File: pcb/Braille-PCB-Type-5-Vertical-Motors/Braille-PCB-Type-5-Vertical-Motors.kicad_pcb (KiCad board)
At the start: 2 copper layers, 90 x 90 mm, 113 parts, among them J1 Screw_Terminal_01x02, J10 Conn_01x02, J11 Conn_01x02, J12 Conn_01x02, J13 Conn_01x02, J14 Conn_01x02, J15 Conn_01x02, J16 Conn_01x02, J17 Conn_01x02, J18 Conn_01x02, J19 Conn_01x02, J2 Screw_Terminal_01x02, J20 Conn_01x02, J3 Screw_Terminal_01x02, J4 Conn_01x03, J5 Conn_01x02, J6 Conn_01x08, J7 Jumper-3-Way-Power, J8 Barrel_Jack_Switch, J9 Conn_01x02, M1 Motor_DC, M10 Motor_DC, M11 Motor_DC, M12 Motor_DC, M2 Motor_DC, M3 Motor_DC, M4 Motor_DC, M5 Motor_DC, M6 Motor_DC, M7 Motor_DC, M8 Motor_DC, M9 Motor_DC, SW1 SW_Push, SW2 SW_Push, U1 RP2040-Zero, U10 AD116, U14 AD116, U15 AD116, U16 AD116, U2 AD116, U20 AD116, U21 AD116, U22 AD116, U26 74HC595, U27 74HC595, U28 74HC595, U3 AD116, U32 AMS1117-3.3, U4 AD116, U8 AD116, U9 AD116

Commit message: PCB WIP: Add motor shaft holes
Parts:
- added H13: MountingHole, 00-project-footprints:Hole_for_Motor_Shaft, F.Cu at (52.7, 47.4)
- added H14: MountingHole, 00-project-footprints:Hole_for_Motor_Shaft, F.Cu at (154.9, 72.3)
- added H15: MountingHole, 00-project-footprints:Hole_for_Motor_Shaft, F.Cu at (162.7, 72.3)
- added H16: MountingHole, 00-project-footprints:Hole_for_Motor_Shaft, F.Cu at (170.4, 72.3)
- added H17: MountingHole, 00-project-footprints:Hole_for_Motor_Shaft, F.Cu at (49.7, 50.0)
- added H18: MountingHole, 00-project-footprints:Hole_for_Motor_Shaft, F.Cu at (154.9, 78.0)
- added H19: MountingHole, 00-project-footprints:Hole_for_Motor_Shaft, F.Cu at (162.7, 78.0)
- added H20: MountingHole, 00-project-footprints:Hole_for_Motor_Shaft, F.Cu at (170.4, 78.0)
- added H21: MountingHole, 00-project-footprints:Hole_for_Motor_Shaft, F.Cu at (52.7, 52.6)
- added H22: MountingHole, 00-project-footprints:Hole_for_Motor_Shaft, F.Cu at (154.9, 83.8)
- added H23: MountingHole, 00-project-footprints:Hole_for_Motor_Shaft, F.Cu at (162.7, 83.8)
- added H24: MountingHole, 00-project-footprints:Hole_for_Motor_Shaft, F.Cu at (170.4, 83.8)
- D1, D26, D27: footprint LED_SMD:LED_1206_3216Metric_Pad1.42x1.75mm_HandSolder -> LED_SMD:LED_0603_1608Metric_Pad1.05x0.95mm_HandSolder
- moved J19 117.8 mm to (63.2, 69.5), turned to -90 degrees
- moved J15 113.0 mm to (63.2, 65.5), turned to -90 degrees
- moved J11 108.2 mm to (63.2, 61.5), turned to -90 degrees
- moved J20 100.0 mm to (69.2, 69.5), turned to -90 degrees
- moved J16 95.3 mm to (69.2, 65.5), turned to -90 degrees
- moved M3 93.6 mm to (61.7, 47.4), turned to 180 degrees
- moved M7 90.9 mm to (64.7, 50.0), turned to 180 degrees
- moved J18 90.7 mm to (57.2, 69.5), turned to -90 degrees
- moved J12 90.7 mm to (69.2, 61.5), turned to -90 degrees
- moved M11 89.0 mm to (61.7, 52.6), turned to 180 degrees
- moved J14 86.4 mm to (57.2, 65.5), turned to -90 degrees
- moved J10 82.4 mm to (57.2, 61.5), turned to -90 degrees
- moved M4 76.1 mm to (67.7, 47.4), turned to 180 degrees
- moved M8 73.6 mm to (70.7, 50.0), turned to 180 degrees
- moved M12 71.5 mm to (67.7, 52.6), turned to 180 degrees
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
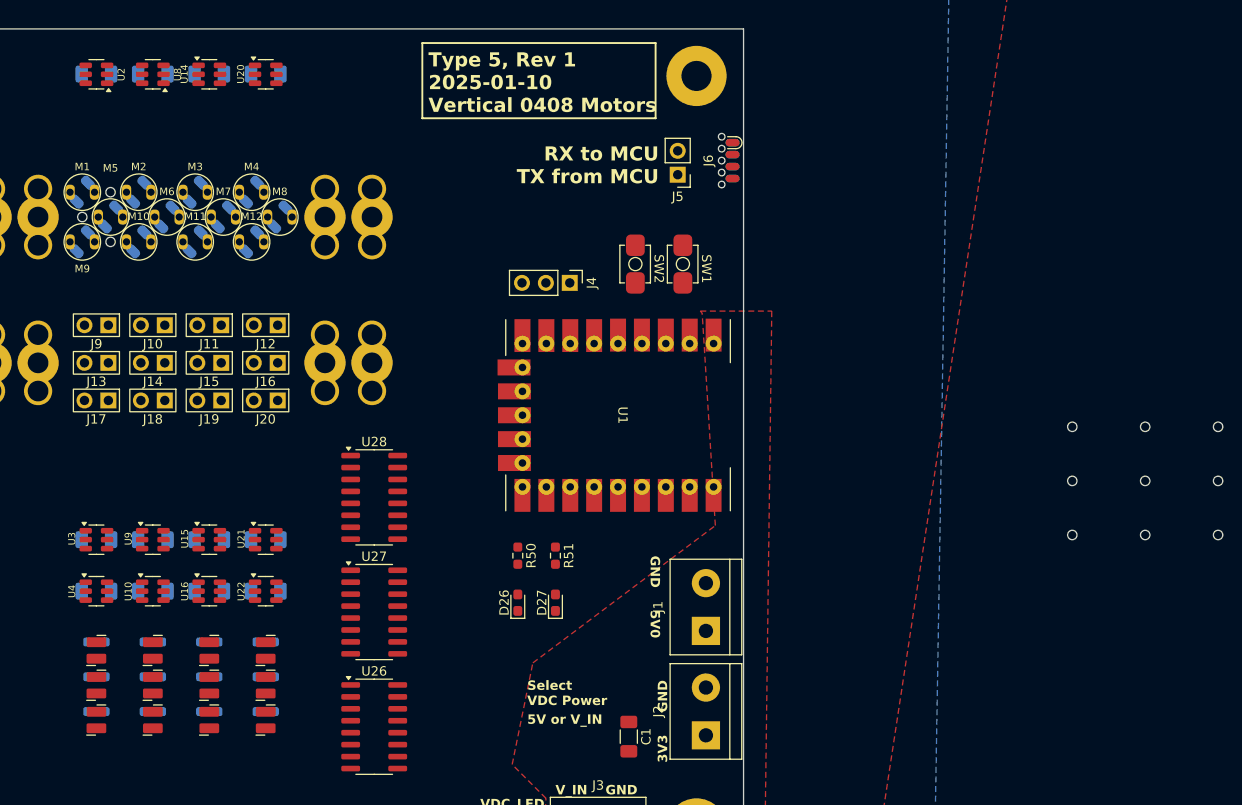
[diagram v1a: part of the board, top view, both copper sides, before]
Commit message: PCB WIP: More layout
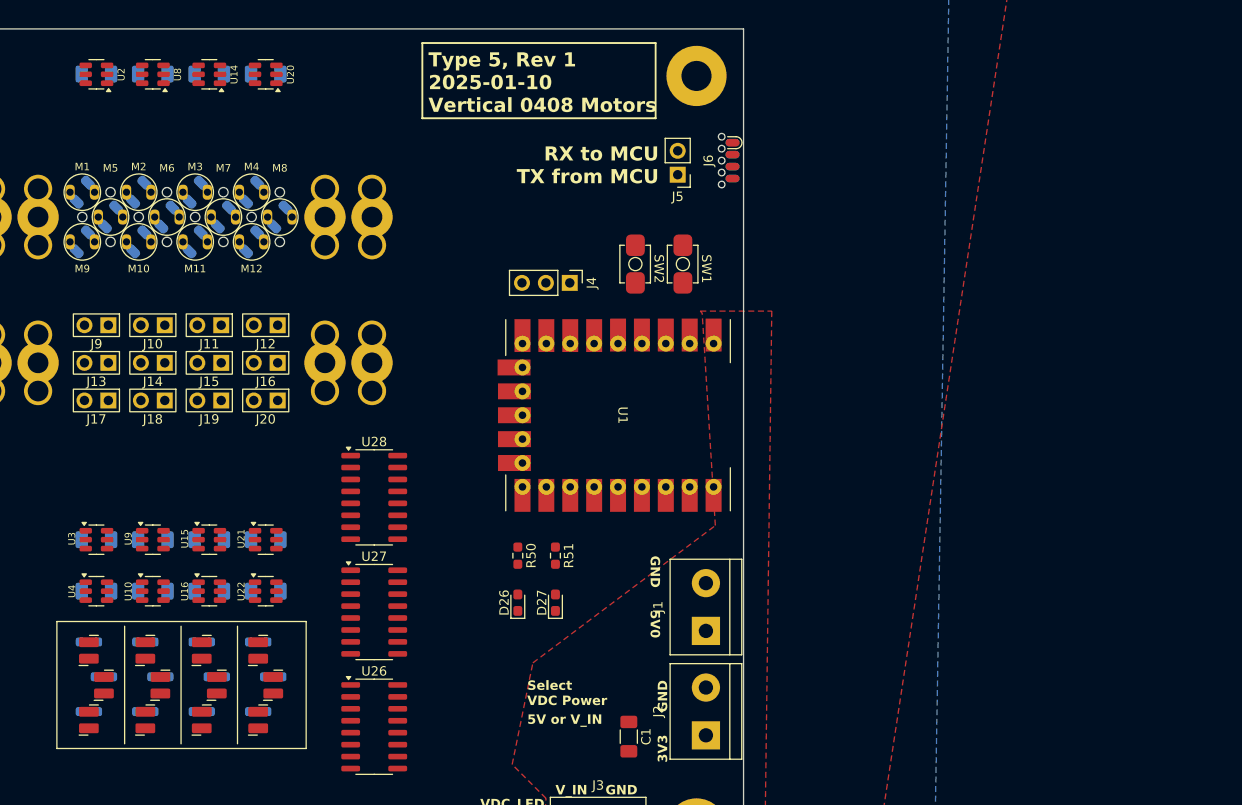
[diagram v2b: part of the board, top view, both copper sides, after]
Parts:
- moved H20 106.5 mm to (67.7, 50.0)
- moved H19 104.8 mm to (61.7, 50.0)
- moved H24 104.5 mm to (70.7, 52.6)
- moved H18 103.1 mm to (55.7, 50.0)
- moved H23 102.8 mm to (64.7, 52.6)
- moved H16 102.8 mm to (70.7, 47.4)
- moved H22 101.2 mm to (58.7, 52.6)
- moved H15 101.1 mm to (64.7, 47.4)
- moved H14 99.4 mm to (58.7, 47.4)
- moved D10 0.80 mm to (56.4, 103.5)
- moved D14 0.80 mm to (62.4, 96.1)
- moved D16 0.80 mm to (62.4, 103.5)
- moved D2 0.80 mm to (50.4, 96.1)
- moved D4 0.80 mm to (50.4, 103.5)
- moved D8 0.80 mm to (56.4, 96.1)
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
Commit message: PCB: Add cross-PCB connectors
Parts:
- added J21: Conn_01x05, 00-project-footprints:PinHeader_1x05_P2.54mm_Vertical_Tight_Centered, F.Cu at (85.5, 50.0)
- added J22: Conn_01x05, 00-project-footprints:PinHeader_1x05_P2.54mm_Vertical_Tight_Centered, F.Cu at (88.5, 50.0)
- added J23: Conn_01x05, 00-project-footprints:PinHeader_1x05_P2.54mm_Vertical_Tight_Centered, F.Cu at (32.0, 50.0)
- added J24: Conn_01x05, 00-project-footprints:PinHeader_1x05_P2.54mm_Vertical_Tight_Centered, F.Cu at (35.0, 50.0)
- moved C31 107.6 mm to (86.6, 99.5)
- moved C30 98.1 mm to (86.6, 87.5)
- moved C27 88.2 mm to (86.6, 75.0)
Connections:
- U28 pad 9: unconnected-(U28-QH'-Pad9) -> /SHIFT_SER_OUT
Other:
- board text added: "IN"
- board text added: "OUT"

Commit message: PCB: Finish setting up power planes
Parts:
- H1, H2, H3, H4: footprint MountingHole:MountingHole_3.2mm_M3_Pad -> 00-project-footprints:MountingHole_M3_2x_3mm_Pitch
- moved J8 163.4 mm to (90.5, 112.0), turned to 90 degrees
- moved JP1 149.8 mm to (96.0, 101.5)
- moved J7 145.7 mm to (81.0, 114.0)
- moved U32 144.1 mm to (56.0, 113.0), turned to 180 degrees
- moved C29 142.9 mm to (62.0, 116.0), turned to -90 degrees
- moved C28 140.7 mm to (62.0, 110.5), turned to -90 degrees
- moved C26 133.2 mm to (108.0, 91.0), turned to 90 degrees
- moved C31 58.9 mm to (35.0, 71.1), turned to 90 degrees
- moved U26 49.0 mm to (40.0, 77.0), turned to 90 degrees
- moved D1 48.7 mm to (47.0, 112.6)
- moved R1 48.7 mm to (47.0, 116.5)
- moved C1 2.34 mm to (108.5, 103.0), turned to 90 degrees
- moved SW1 2.05 mm to (111.5, 55.0)
- moved SW2 2.05 mm to (106.5, 55.0)
- moved J3 1.54 mm to (100.5, 115.5)
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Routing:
- net +5V: track 0.00 -> 58.7 mm
- net +3V3: track 0.00 -> 53.3 mm
- net Net-(JP1-C): track 0.00 -> 39.6 mm
- net Net-(J3-Pin_1): track 0.00 -> 28.3 mm
- net Net-(J7-IN2): track 0.00 -> 26.4 mm
- net /SW_1: track 0.00 -> 8.46 mm
- net /GP_LED_0: track 0.00 -> 6.83 mm
- net /GP_LED_1: track 0.00 -> 6.61 mm
- net /SW_2: track 0.00 -> 6.57 mm
- net Net-(J4-Pin_2): track 0.00 -> 6.47 mm
- net Net-(J4-Pin_1): track 0.00 -> 6.47 mm
- net /UART0_TX: track 0.00 -> 6.19 mm
- net /UART0_RX: track 0.00 -> 6.00 mm
- net Net-(J4-Pin_3): track 0.00 -> 5.62 mm
- net Net-(D1-A): track 0.00 -> 3.96 mm
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- added copper zone on B.Cu, net GND
- added copper zone on B.Cu, net VDC
- removed copper zone on F.Cu, net +5V
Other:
- board text added: "2.5mm Intra-Cell Pitch. 6mm Inter-Cell Pitch X. Motor Pitch X: 3mm. Motor Pitch Y: 2.64mm. Top (Red) = GND Bottom (Blue) = VDC"
- board text added: "3 - V_IN 2 - LDO 1 - RP-3V3"
- board text added: "5V"
- board text added: "Pick LDO Input"
- board text added: "Pick VDC Driver"
- board text added: "V_IN"
- board text removed: "2.5mm Intra-Cell Pitch. 6mm Inter-Cell Pitch X. Motor Pitch X: 3mm. Motor Pitch Y: 2.64mm. Top (Red) = GND Bottom (Blue) = 3V3"
- board text removed: "5V or V_IN"
- board text removed: "Select VDC Power"

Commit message: Finish Type 5 Rev 1 PCB
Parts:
- moved H1 1.50 mm to (36.5, 35.0)
- moved H2 1.50 mm to (113.5, 35.0)
- moved H3 1.50 mm to (36.5, 114.0)
- moved H4 1.50 mm to (113.5, 115.0)
- turned C14 to 0 degrees
- turned C2 to 0 degrees
- turned C20 to 0 degrees
- turned C8 to 0 degrees
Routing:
- net GND: track 0.00 -> 340.3 mm, vias 13 -> 50
- net VDC: track 1.04 -> 201.0 mm, vias 1 -> 28
- net /Braille_Cells_and_Controls/CELL1_DOT1_B: track 0.00 -> 169.2 mm, vias 0 -> 6
- net /SHIFT_SRCK: track 0.00 -> 136.5 mm, vias 0 -> 8
- net /~{SHIFT_OE}: track 0.00 -> 133.5 mm, vias 0 -> 7
- net /SHIFT_SER_IN: track 0.00 -> 131.3 mm, vias 0 -> 3
- net /~{SHIFT_SRCLR}: track 0.00 -> 128.8 mm, vias 0 -> 6
- net /Braille_Cells_and_Controls/CELL2_DOT1_A: track 0.00 -> 122.6 mm, vias 0 -> 5
- net /Braille_Cells_and_Controls/CELL2_DOT1_B: track 0.00 -> 122.2 mm, vias 0 -> 4
- net /SHIFT_RCLK: track 0.00 -> 116.3 mm, vias 0 -> 4
- net /Braille_Cells_and_Controls/CELL3_DOT1_B: track 0.00 -> 103.4 mm, vias 0 -> 4
- net +3V3: track 53.3 -> 141.7 mm, vias 0 -> 10
- net /Braille_Cells_and_Controls/CELL1_DOT1_A: track 0.00 -> 88.1 mm, vias 0 -> 4
- net /Braille_Cells_and_Controls/CELL0_DOT1_B: track 0.00 -> 81.9 mm, vias 0 -> 2
- net /Braille_Cells_and_Controls/CELL3_DOT1_A: track 0.00 -> 79.3 mm, vias 0 -> 4
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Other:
- board text added: "Type 5 Rev 1 2025-01-10 Vertical 0408 Motors"
- board text removed: "Type 5, Rev 1 2025-01-10 Vertical 0408 Motors"

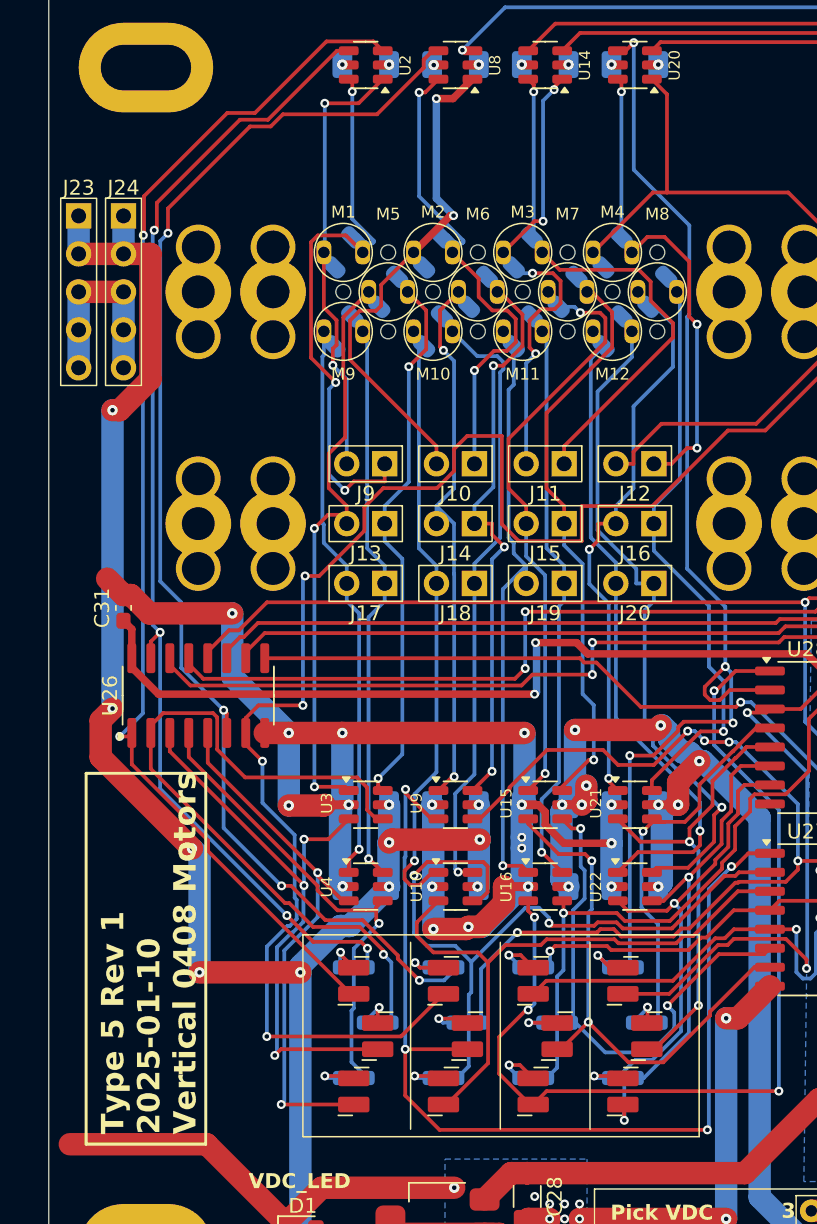
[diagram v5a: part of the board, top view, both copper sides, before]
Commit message: PCB Rev 2: Increase shaft hole diameter from 1mm to 2mm
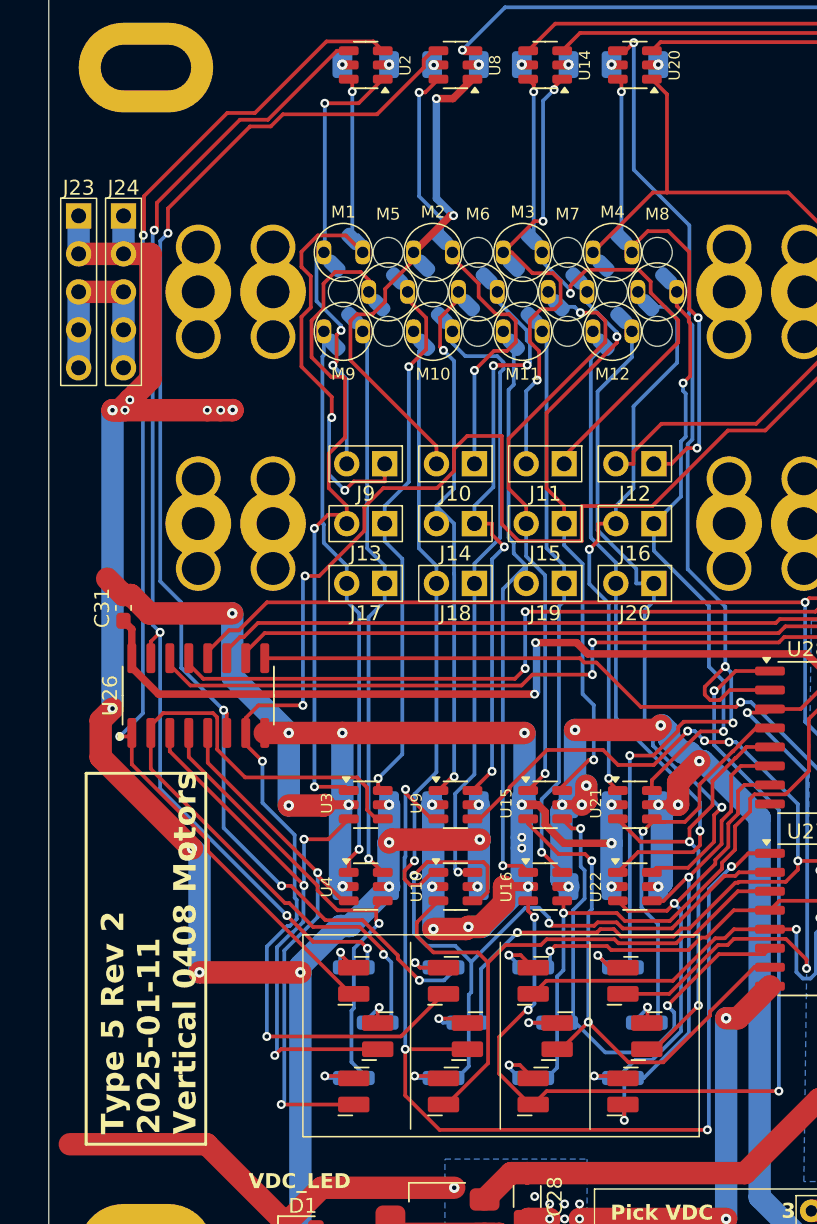
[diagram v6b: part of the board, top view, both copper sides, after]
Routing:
- net VDC: track 201.0 -> 209.0 mm, vias 28 -> 33
- net /Braille_Cells_and_Controls/Braille_Cell/DOT2_B: track 40.7 -> 46.6 mm
- net /Braille_Cells_and_Controls/Braille_Cell1/DOT1_A: track 34.1 -> 31.6 mm
- net /Braille_Cells_and_Controls/Braille_Cell2/DOT1_A: track 36.0 -> 38.4 mm, vias 1 -> 2
- net /Braille_Cells_and_Controls/Braille_Cell1/DOT2_A: track 39.6 -> 41.6 mm, vias 3 -> 4
- net /Braille_Cells_and_Controls/Braille_Cell3/DOT2_A: track 40.3 -> 41.4 mm, vias 1 -> 2
- net /Braille_Cells_and_Controls/Braille_Cell/DOT1_B: track 30.9 -> 31.9 mm, vias 2 -> 3
- net /Braille_Cells_and_Controls/Braille_Cell3/DOT1_A: track 32.9 -> 34.0 mm
- net /Braille_Cells_and_Controls/Braille_Cell3/DOT2_B: track 38.4 -> 39.0 mm
- net /Braille_Cells_and_Controls/Braille_Cell2/DOT2_A: track 39.7 -> 40.0 mm, vias 1 -> 2
- net /Braille_Cells_and_Controls/Braille_Cell2/DOT1_B: vias 4 -> 3
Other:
- board text added: "Type 5 Rev 2 2025-01-11 Vertical 0408 Motors"
- board text removed: "Type 5 Rev 1 2025-01-10 Vertical 0408 Motors"

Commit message: PCB: Work on new revision
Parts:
- removed D10, D14, D15, D16, D2, D20, D21, D22, D3, D4, D8, D9: LED_Dual_Bidirectional, 00-project-footprints:LED_0603_1608Metric_HandSolder_2x_Reverse
- removed J4: Conn_01x03, Connector_PinHeader_2.54mm:PinHeader_1x03_P2.54mm_Vertical
- removed J7: Jumper-3-Way-Power, 00-project-footprints:Jumper-3-Way-2.54mm-Headers
- removed J8: Barrel_Jack_Switch, Connector_BarrelJack:BarrelJack_Horizontal
- removed JP1: Jumper_3_Open, Connector_PinHeader_2.54mm:PinHeader_1x03_P2.54mm_Vertical
- removed M1, M10, M11, M12, M2, M3, M4, M5, M6, M7, M8, M9: Motor_DC, 00-project-footprints:Motor_Tiny_0408_Vertical
- removed R10, R21, R22, R33, R34, R45, R46, R9: 5k1, Resistor_SMD:R_0603_1608Metric_Pad0.98x0.95mm_HandSolder
- added C103: 100n, Capacitor_SMD:C_0603_1608Metric_Pad1.08x0.95mm_HandSolder, F.Cu at (164.5, 99.2)
- added D201: LED_Dual_AAKK, 00-project-footprints:LED_1206_Bicolor_AAKK, F.Cu at (168.1, 82.8)
- added D202: LED_Dual_AAKK, 00-project-footprints:LED_1206_Bicolor_AAKK, F.Cu at (168.1, 86.6)
- added D203: LED_Dual_AAKK, 00-project-footprints:LED_1206_Bicolor_AAKK, F.Cu at (168.1, 90.5)
- added D301: LED_Dual_AAKK, 00-project-footprints:LED_1206_Bicolor_AAKK, F.Cu at (152.2, 65.7)
- added D302: LED_Dual_AAKK, 00-project-footprints:LED_1206_Bicolor_AAKK, F.Cu at (152.2, 69.5)
- added D303: LED_Dual_AAKK, 00-project-footprints:LED_1206_Bicolor_AAKK, F.Cu at (152.2, 73.4)
- added D401: LED_Dual_AAKK, 00-project-footprints:LED_1206_Bicolor_AAKK, F.Cu at (168.1, 65.7)
- added D402: LED_Dual_AAKK, 00-project-footprints:LED_1206_Bicolor_AAKK, F.Cu at (168.1, 69.5)
- added D403: LED_Dual_AAKK, 00-project-footprints:LED_1206_Bicolor_AAKK, F.Cu at (168.1, 73.4)
- added D501: LED_Dual_AAKK, 00-project-footprints:LED_1206_Bicolor_AAKK, F.Cu at (152.2, 82.8)
- added D502: LED_Dual_AAKK, 00-project-footprints:LED_1206_Bicolor_AAKK, F.Cu at (152.2, 86.6)
- added D503: LED_Dual_AAKK, 00-project-footprints:LED_1206_Bicolor_AAKK, F.Cu at (152.2, 90.5)
- added H204: MountingHole, 00-project-footprints:Hole_for_Motor_Shaft, F.Cu at (163.8, 82.3)
- added H205: MountingHole, 00-project-footprints:Hole_for_Motor_Shaft, F.Cu at (163.8, 85.3)
- added H206: MountingHole, 00-project-footprints:Hole_for_Motor_Shaft, F.Cu at (163.8, 88.3)
- added H304: MountingHole, 00-project-footprints:Hole_for_Motor_Shaft, F.Cu at (147.9, 68.2)
- added H305: MountingHole, 00-project-footprints:Hole_for_Motor_Shaft, F.Cu at (147.9, 71.2)
- added H306: MountingHole, 00-project-footprints:Hole_for_Motor_Shaft, F.Cu at (147.9, 74.2)
- added H404: MountingHole, 00-project-footprints:Motor_Tiny_0408_Vertical, F.Cu at (163.8, 65.2)
- added H405: MountingHole, 00-project-footprints:Hole_for_Motor_Shaft, F.Cu at (163.8, 68.2)
- added H406: MountingHole, 00-project-footprints:Hole_for_Motor_Shaft, F.Cu at (163.8, 71.2)
- added H407: MountingHole, 00-project-footprints:Hole_for_Motor_Shaft, F.Cu at (163.8, 74.2)
- added H504: MountingHole, 00-project-footprints:Motor_Tiny_0408_Vertical, F.Cu at (147.9, 82.3)
- added H505: MountingHole, 00-project-footprints:Hole_for_Motor_Shaft, F.Cu at (147.9, 85.3)
- added H506: MountingHole, 00-project-footprints:Hole_for_Motor_Shaft, F.Cu at (147.9, 88.3)
- added H507: MountingHole, 00-project-footprints:Hole_for_Motor_Shaft, F.Cu at (147.9, 91.3)
- added M201: MountingHole, 00-project-footprints:Motor_Tiny_0408_Vertical, F.Cu at (49.7, 47.0)
- added M202: MountingHole, 00-project-footprints:Motor_Tiny_0408_Vertical, F.Cu at (52.7, 50.0)
- added M203: MountingHole, 00-project-footprints:Motor_Tiny_0408_Vertical, F.Cu at (49.7, 53.0)
- added M301: MountingHole, 00-project-footprints:Motor_Tiny_0408_Vertical, F.Cu at (147.9, 65.2)
- added M302: MountingHole, 00-project-footprints:Motor_Tiny_0408_Vertical, F.Cu at (157.7, 66.2)
- added M303: MountingHole, 00-project-footprints:Motor_Tiny_0408_Vertical, F.Cu at (157.7, 71.3)
- added M401: MountingHole, 00-project-footprints:Motor_Tiny_0408_Vertical, F.Cu at (173.7, 66.2)
- added M402: MountingHole, 00-project-footprints:Motor_Tiny_0408_Vertical, F.Cu at (173.7, 71.3)
- added M501: MountingHole, 00-project-footprints:Motor_Tiny_0408_Vertical, F.Cu at (157.7, 83.3)
- added M502: MountingHole, 00-project-footprints:Motor_Tiny_0408_Vertical, F.Cu at (157.7, 88.4)
- added R103: R, Resistor_SMD:R_1206_3216Metric_Pad1.30x1.75mm_HandSolder, F.Cu at (169.7, 106.2)
- added R105: 5k1, Resistor_SMD:R_0603_1608Metric_Pad0.98x0.95mm_HandSolder, F.Cu at (164.5, 101.7)
- added R106: 5k1, Resistor_SMD:R_0603_1608Metric_Pad0.98x0.95mm_HandSolder, F.Cu at (164.5, 104.2)
- added R202: 5k1, Resistor_SMD:R_0603_1608Metric_Pad0.98x0.95mm_HandSolder, F.Cu at (173.1, 92.2)
- added R203: 5k1, Resistor_SMD:R_0603_1608Metric_Pad0.98x0.95mm_HandSolder, F.Cu at (173.1, 94.7)
- added R302: 5k1, Resistor_SMD:R_0603_1608Metric_Pad0.98x0.95mm_HandSolder, F.Cu at (157.1, 75.1)
- added R303: 5k1, Resistor_SMD:R_0603_1608Metric_Pad0.98x0.95mm_HandSolder, F.Cu at (157.1, 77.6)
- added R402: 5k1, Resistor_SMD:R_0603_1608Metric_Pad0.98x0.95mm_HandSolder, F.Cu at (173.1, 75.1)
- added R403: 5k1, Resistor_SMD:R_0603_1608Metric_Pad0.98x0.95mm_HandSolder, F.Cu at (173.1, 77.6)
- added R502: 5k1, Resistor_SMD:R_0603_1608Metric_Pad0.98x0.95mm_HandSolder, F.Cu at (157.1, 92.2)
- added R503: 5k1, Resistor_SMD:R_0603_1608Metric_Pad0.98x0.95mm_HandSolder, F.Cu at (157.1, 94.7)
- added U103: INA219AxD, Package_SO:SOIC-8_3.9x4.9mm_P1.27mm, F.Cu at (170.9, 101.3)
- moved H109 30.0 mm to (40.0, 95.5)
- moved H110 30.0 mm to (45.0, 95.5)
- moved H111 30.0 mm to (75.5, 95.5)
- moved H112 30.0 mm to (80.5, 95.5)
- moved J201 20.7 mm to (50.2, 40.8), turned to 90 degrees
- moved C202 8.00 mm to (51.2, 76.3)
- moved C203 8.00 mm to (51.2, 81.8)
- moved C302 8.00 mm to (57.2, 76.3)
- moved C303 8.00 mm to (57.2, 81.8)
- moved C402 8.00 mm to (63.2, 76.3)
- moved C403 8.00 mm to (63.2, 81.8)
- moved C502 8.00 mm to (69.2, 76.3)
- moved C503 8.00 mm to (69.2, 81.8)
- moved U202 8.00 mm to (51.2, 76.3)
- moved U203 8.00 mm to (51.2, 81.8)
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- renumbered C1 to C101, C26 to C102, C28 to C104, C29 to C105, C2 to C201, C3 to C202, C4 to C203, C8 to C301, C9 to C302, C10 to C303, C14 to C401, C15 to C402, C16 to C403, C20 to C501, C21 to C502, C22 to C503, C27 to C601, C30 to C602, C31 to C603, D27 to D101, D26 to D102, D1 to D103, H1 to H101, H2 to H102, H3 to H103, H4 to H104, H5 to H105, H9 to H106, H6 to H107, H10 to H108, H7 to H109, H8 to H110, H11 to H111, H12 to H112, H13 to H201, H17 to H202, H21 to H203, H14 to H301, H18 to H302, H22 to H303, H15 to H401, H19 to H402, H23 to H403, H16 to H501, H20 to H502, H24 to H503, J5 to J101, J1 to J102, J2 to J103, J3 to J104, J21 to J105, J22 to J106, J6 to J107, J23 to J108, J24 to J109, J9 to J201, J13 to J202, J17 to J203, J10 to J301, J14 to J302, J18 to J303, J11 to J401, J15 to J402, J19 to J403, J12 to J501, J16 to J502, J20 to J503, R51 to R101, R50 to R102, R1 to R104, R8 to R201, R20 to R301, R32 to R401, R44 to R501, SW1 to SW101, SW2 to SW102, U1 to U101, U32 to U102, U2 to U201, U3 to U202, U4 to U203, U8 to U301, U9 to U302, U10 to U303, U14 to U401, U15 to U402, U16 to U403, U20 to U501, U21 to U502, U22 to U503, U26 to U601, U27 to U602, U28 to U603
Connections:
- C104 pad 1: Net-(JP1-C) -> +5V
- J104 pad 1: Net-(J3-Pin_1) -> VDC
- U101 pad 7: Net-(J4-Pin_1) -> unconnected-(U101-GP26-Pad7)
- U101 pad 8: Net-(J4-Pin_2) -> I2C_SCL
- U101 pad 9: Net-(J4-Pin_3) -> I2C_SDA
- U102 pad 3: Net-(JP1-C) -> +5V
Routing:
- net GND: track 340.3 -> 222.0 mm, vias 50 -> 30
- net /Braille_Cells_and_Controls/CELL1_DOT1_B: track 169.2 -> 54.8 mm, vias 6 -> 1
- net /Braille_Cells_and_Controls/CELL1_DOT1_A: track 88.1 -> 0.00 mm, vias 4 -> 0
- net VDC: track 209.0 -> 122.0 mm, vias 33 -> 6
- net /Braille_Cells_and_Controls/CELL3_DOT1_A: track 79.4 -> 0.00 mm, vias 4 -> 0
- net /Braille_Cells_and_Controls/CELL0_DOT1_A: track 78.1 -> 0.00 mm, vias 4 -> 0
- net /SHIFT_SRCK: track 136.5 -> 58.9 mm, vias 8 -> 4
- net /Braille_Cells_and_Controls/CELL1_DOT2_B: track 70.2 -> 1.44 mm, vias 4 -> 0
- net /~{SHIFT_SRCLR}: track 128.8 -> 62.5 mm, vias 6 -> 4
- net /SHIFT_RCLK: track 116.3 -> 52.2 mm, vias 4 -> 2
- net +3V3: track 141.7 -> 85.3 mm, vias 10 -> 7
- net /Braille_Cells_and_Controls/Braille_Cell3/DOT1_B: track 54.3 -> 0.00 mm
- net /Braille_Cells_and_Controls/CELL0_DOT1_B: track 81.9 -> 31.9 mm, vias 2 -> 0
- net /SHIFT_SER_IN: track 131.3 -> 81.6 mm, vias 3 -> 1
- net /Braille_Cells_and_Controls/CELL0_DOT2_A: track 49.5 -> 0.00 mm, vias 1 -> 0
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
